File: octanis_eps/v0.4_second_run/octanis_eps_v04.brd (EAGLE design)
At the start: 63.7 x 49.6 mm, 107 parts, among them IC1 OPA2333DGK, IC100 OPA2333DGK, IC101 OPA347, IC2 OPA2333DGK, Q1 N-HEXFET-2D_SOT232-, Q100 N-HEXFET-2D_SOT232-, Q2 N-HEXFET-2D_SOT232-, Q3 FC-12M

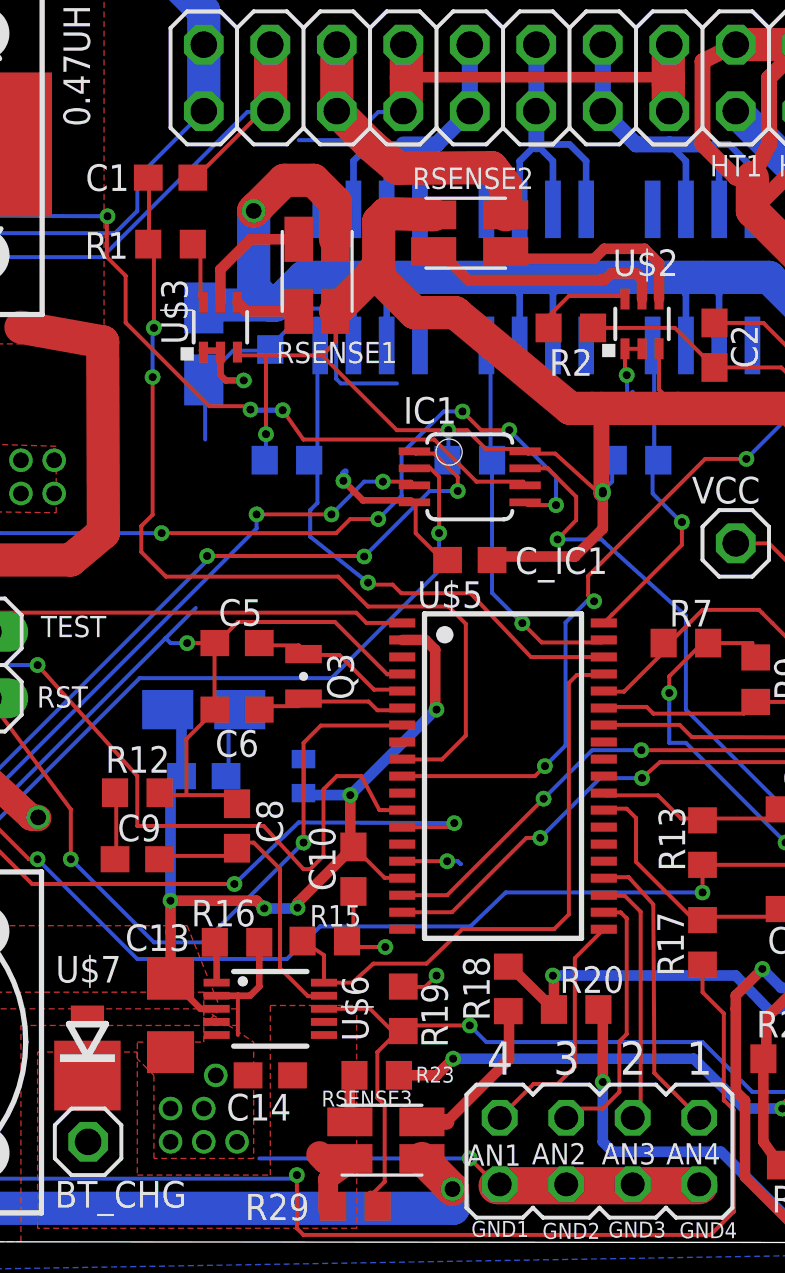
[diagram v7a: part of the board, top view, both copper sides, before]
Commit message: minor eps changes. stencil laser cut files for v0.6 added
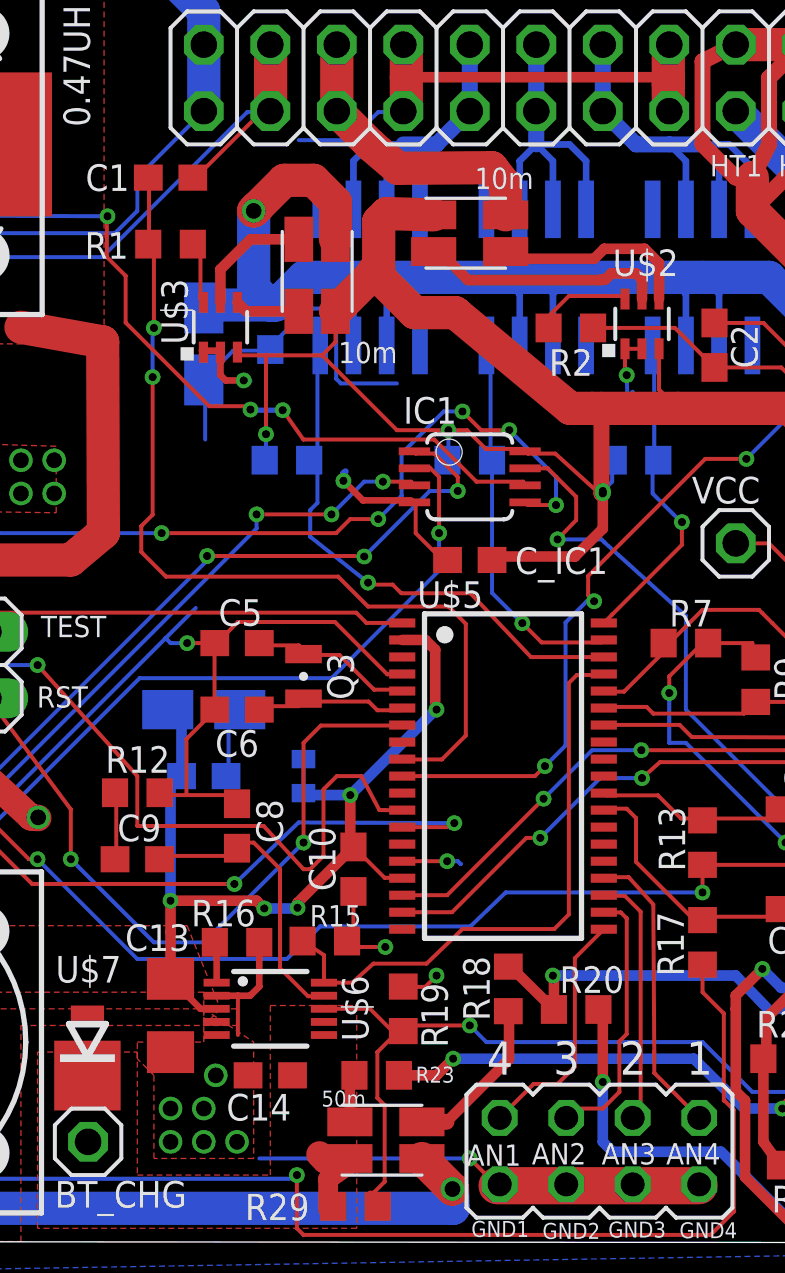
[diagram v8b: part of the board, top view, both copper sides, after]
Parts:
- C13: value 4.7u -> 4.7uF
- C14, C4: value 22u -> 22uF
- C3: value 10u -> 10uF
- C8: value 4.7p -> 4.7pF
- C9: value 470p -> 470pF
- RSENSE1: value RSENSE2 -> 10m
- RSENSE2: value RSENSE3 -> 50m
- R_SENSE1: value RSENSE1 -> 10m
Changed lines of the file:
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@@
 <attribute name="VALUE" x="6.35" y="58.42" size="1.27" layer="27" rot="R180"/>
 </element>
-<element name="C13" library="rcl" package="C1206" value="4.7u" x="19.05" y="39.116" smashed="yes" rot="R90">
+<element name="C13" library="rcl" package="C1206" value="4.7uF" x="19.05" y="39.116" smashed="yes" rot="R90">
 <attribute name="NAME" x="19.7866" y="42.5958" size="1.016" layer="25" rot="R180"/>
 <attribute name="VALUE" x="21.59" y="37.846" size="1.27" layer="27" rot="R90"/>
 </element>
-<element name="C9" library="rcl" package="C0603" value="470p" x="17.78" y="45.085" smashed="yes">
+<element name="C9" library="rcl" package="C0603" value="470pF" x="17.78" y="45.085" smashed="yes">
 <attribute name="NAME" x="17.018" y="45.7708" size="1.016" layer="25"/>
 <attribute name="VALUE" x="17.145" y="43.18" size="1.27" layer="27"/>
 </element>
-<element name="C14" library="rcl" package="C0603" value="22u" x="22.86" y="36.83" smashed="yes">
+<element name="C14" library="rcl" package="C0603" value="22uF" x="22.86" y="36.83" smashed="yes">
 <attribute name="NAME" x="21.1836" y="35.1028" size="1.016" layer="25"/>
 <attribute name="VALUE" x="22.225" y="34.925" size="1.27" layer="27"/>
@@
 <attribute name="VALUE" x="17.145" y="45.72" size="1.27" layer="27"/>
 </element>
-<element name="C3" library="rcl" package="C1206" value="10u" x="6.35" y="63.5" smashed="yes" rot="R180">
+<element name="C3" library="rcl" package="C1206" value="10uF" x="6.35" y="63.5" smashed="yes" rot="R180">
 <attribute name="NAME" x="3.7846" y="64.1604" size="1.016" layer="25" rot="R180"/>
 <attribute name="VALUE" x="7.62" y="66.04" size="1.27" layer="27" rot="R180"/>
 </element>
-<element name="C4" library="rcl" package="C1206" value="22u" x="10.16" y="62.23" smashed="yes" rot="R90">
+<element name="C4" library="rcl" package="C1206" value="22uF" x="10.16" y="62.23" smashed="yes" rot="R90">
 <attribute name="NAME" x="12.446" y="61.4172" size="1.016" layer="25" rot="R90"/>
 <attribute name="VALUE" x="12.7" y="60.96" size="1.27" layer="27" rot="R90"/>
 </element>
-<element name="C8" library="rcl" package="C0603" value="4.7p" x="21.59" y="46.355" smashed="yes" rot="R270">
+<element name="C8" library="rcl" package="C0603" value="4.7pF" x="21.59" y="46.355" smashed="yes" rot="R270">
 <attribute name="NAME" x="22.3266" y="47.371" size="1.016" layer="25" rot="R270"/>
 <attribute name="VALUE" x="19.685" y="46.99" size="1.27" layer="27" rot="R270"/>
@@
 <attribute name="VALUE" x="8.128" y="49.3014" size="1.27" layer="27"/>
 </element>
-<element name="R_SENSE1" library="Octanis1_EPS" package="4PADS_RESISTOR" value="RSENSE1" x="25.3492" y="66.0146" smashed="yes" rot="R90">
+<element name="R_SENSE1" library="Octanis1_EPS" package="4PADS_RESISTOR" value="10m" x="25.3492" y="66.0146" smashed="yes" rot="R90">
 <attribute name="VALUE" x="27.7114" y="64.8462" size="0.8128" layer="25" rot="R180"/>
 </element>
-<element name="RSENSE1" library="Octanis1_EPS" package="4PADS_RESISTOR" value="RSENSE2" x="31.8516" y="69.6976" smashed="yes" rot="R180">
+<element name="RSENSE1" library="Octanis1_EPS" package="4PADS_RESISTOR" value="10m" x="31.8516" y="69.6976" smashed="yes" rot="R180">
 <attribute name="VALUE" x="32.9184" y="71.501" size="0.8128" layer="25" rot="R180"/>
 </element>
-<element name="RSENSE2" library="Octanis1_EPS" package="4PADS_RESISTOR" value="RSENSE3" x="28.6512" y="35.052" smashed="yes" rot="R180">
+<element name="RSENSE2" library="Octanis1_EPS" package="4PADS_RESISTOR" value="50m" x="28.6512" y="35.052" smashed="yes" rot="R180">
 <attribute name="VALUE" x="24.8158" y="35.6362" size="0.6096" layer="25"/>
 </element>
